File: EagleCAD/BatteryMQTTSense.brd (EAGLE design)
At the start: 45.5 x 21 mm, 11 parts, among them U2 Si7021-A20

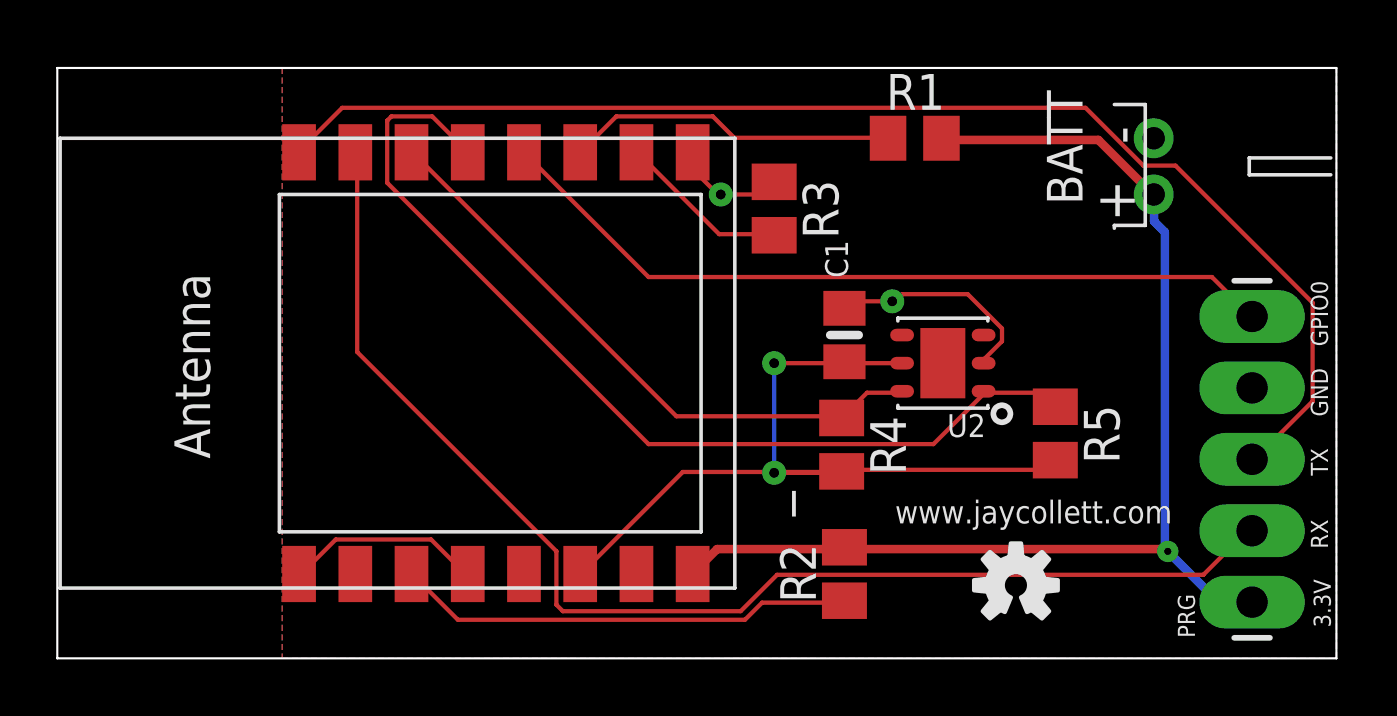
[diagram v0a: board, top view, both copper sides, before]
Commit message: pushing validated version of board and firmware, including stl files for enclosure
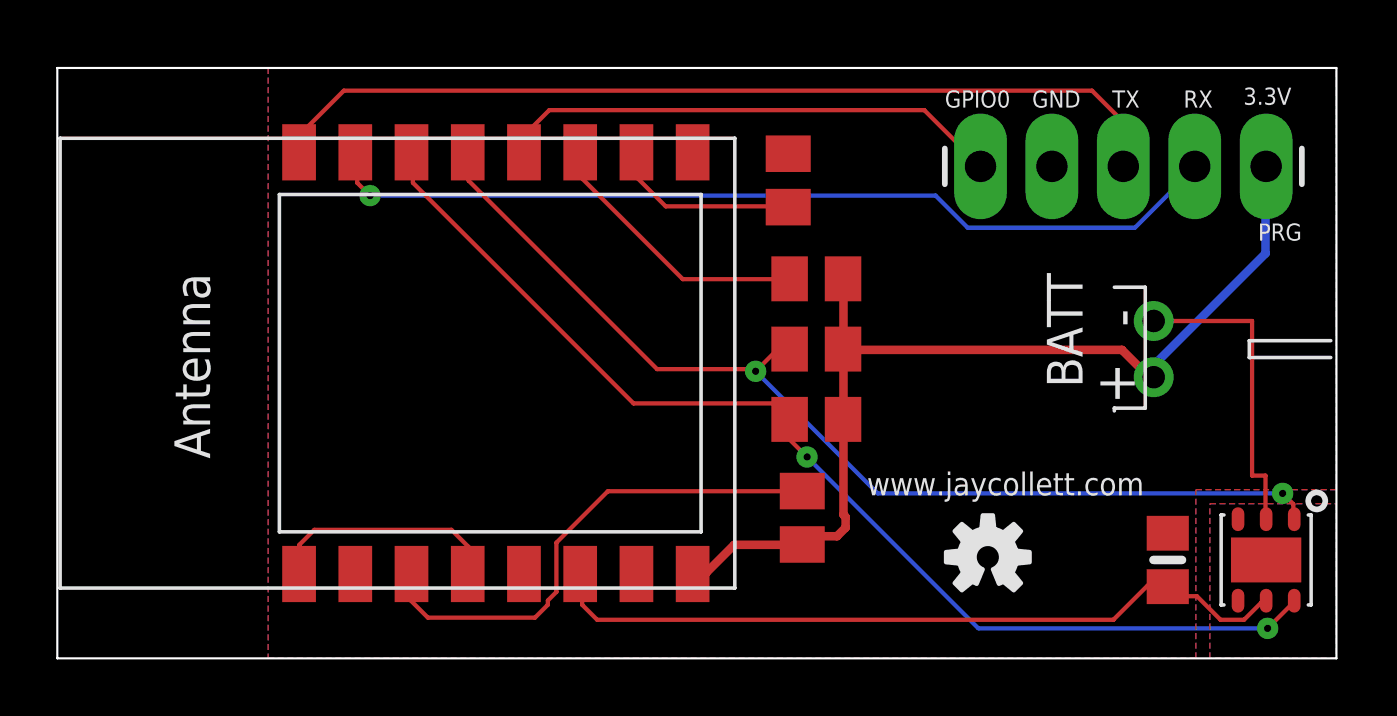
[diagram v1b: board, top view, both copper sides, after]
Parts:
- moved PRG 15.5 mm to (43.0, 17.5), turned to 180 degrees
- moved C1 14.0 mm to (39.5, 3.50)
- moved U2 13.5 mm to (43.0, 3.50), turned to 270 degrees
- moved R5 9.01 mm to (27.0, 11.0), turned to 0 degrees
- moved BATT 6.50 mm to (39.0, 11.0)
- moved R1 6.10 mm to (27.0, 13.5)
- moved R2 2.50 mm to (26.5, 5.00), turned to 270 degrees
- moved LOGO1 1.41 mm to (33.1, 3.60)
- moved R4 1.27 mm to (27.0, 8.50), turned to 0 degrees
- moved R3 1.12 mm to (26.0, 17.0)
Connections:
- net 3.3V: now also R4.2, R5.2
- net SENS_PWR: no longer R4.2, R5.2
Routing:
- net SCL: track 21.8 -> 39.9 mm, vias 0 -> 2
- net TX: track 46.2 -> 32.7 mm
- net RX: track 45.1 -> 32.5 mm, vias 0 -> 1
- net GPIO0: track 28.3 -> 18.1 mm
- net 3.3V: track 42.4 -> 35.6 mm, vias 1 -> 0
- net SDA: track 34.3 -> 37.3 mm, vias 0 -> 2
- net SENS_PWR: track 29.7 -> 27.0 mm, vias 2 -> 0
- net GPIO2: track 11.8 -> 9.85 mm
- net CH_PD: track 16.4 -> 18.1 mm
- net WAKE: track 7.02 -> 8.50 mm
- net GND: track 11.9 -> 11.0 mm, vias 2 -> 0
- net GPIO15: track 6.11 -> 6.74 mm
- added copper zone on layer 1, net ISO
- added copper zone on layer 16, net ISO
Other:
- board text added: "12/29/18"
- board text added: "v2.4"
- board text removed: "12/13/18"
- board text removed: "v2.1"
